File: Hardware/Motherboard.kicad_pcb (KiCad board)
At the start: 2 copper layers, 46 parts, among them J1 BME680, J2 Conn_01x05_Male, J3 Display_1, J4 Display_2, J5 Buttons, J6 USB, Q1 DMG3414U, SW1 Button_Plus, SW2 Button_Minus, SW3 Button_Settings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

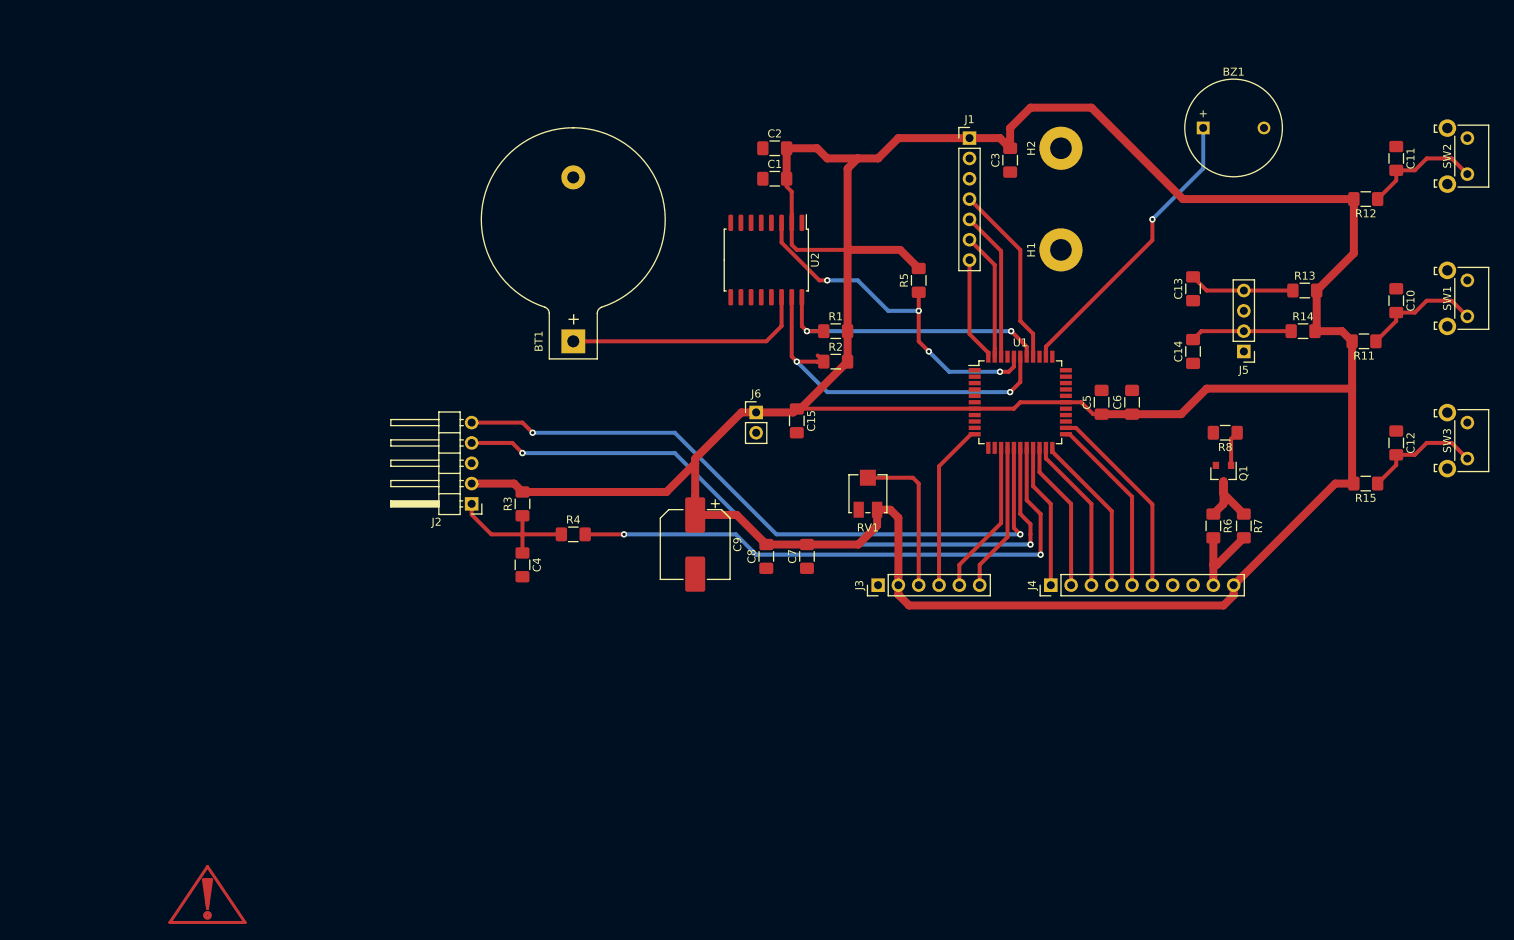
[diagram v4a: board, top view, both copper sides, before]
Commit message: [Hardware] Moved buttons to another schematic sheet and fully routed PCB.
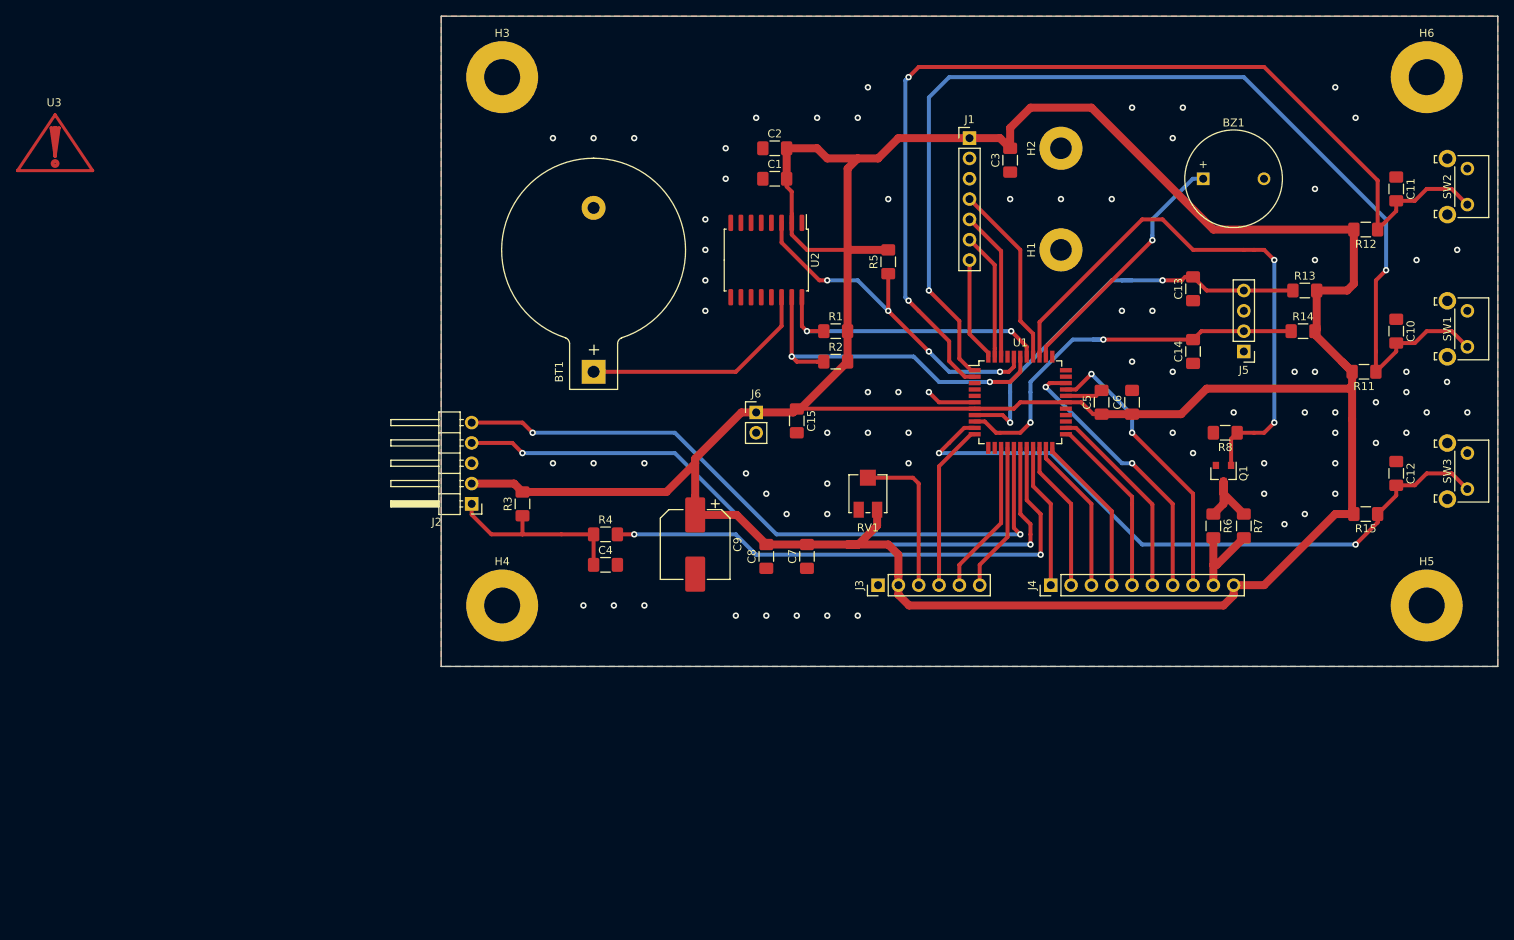
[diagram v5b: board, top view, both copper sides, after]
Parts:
- added H3: MountingHole_Pad, MountingHole:MountingHole_4.5mm_Pad, F.Cu at (128.3, 15.2)
- added H4: MountingHole_Pad, MountingHole:MountingHole_4.5mm_Pad, F.Cu at (128.3, 81.3)
- added H5: MountingHole_Pad, MountingHole:MountingHole_4.5mm_Pad, F.Cu at (243.8, 81.3)
- added H6: MountingHole_Pad, MountingHole:MountingHole_4.5mm_Pad, F.Cu at (243.8, 15.2)
- moved U3 95.9 mm to (72.4, 24.1)
- moved C4 10.4 mm to (141.2, 76.2), turned to 0 degrees
- moved BZ1 6.35 mm to (215.9, 27.9)
- moved BT1 4.58 mm to (139.7, 52.1)
- moved R5 4.46 mm to (176.5, 38.3)
- moved R4 4.03 mm to (141.2, 72.4)
- moved C10 3.81 mm to (240.0, 47.0)
- moved C11 3.81 mm to (240.0, 29.2)
- moved R11 3.81 mm to (236.0, 52.1)
- moved SW1 3.81 mm to (248.9, 44.5)
- moved SW2 3.81 mm to (248.9, 26.7)
- moved R12 3.81 mm to (236.2, 34.3)
- moved C12 3.81 mm to (240.0, 64.8)
- moved SW3 3.81 mm to (248.9, 62.2)
- moved R15 3.81 mm to (236.2, 69.8)
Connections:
- C10 pad 2: Net-(C10-Pad2) -> /PLUS_BUTTON
- C11 pad 2: Net-(C11-Pad2) -> /MINUS_BUTTON
- R11 pad 1: Net-(C10-Pad2) -> /PLUS_BUTTON
- R12 pad 1: Net-(C11-Pad2) -> /MINUS_BUTTON
- SW1 pad 2: Net-(C10-Pad2) -> /PLUS_BUTTON
- SW2 pad 2: Net-(C11-Pad2) -> /MINUS_BUTTON
- U1 pad 1: Net-(U1-Pad1) -> /PLUS_BUTTON
- U1 pad 2: Net-(U1-Pad2) -> /MINUS_BUTTON
- U1 pad 25: Net-(C11-Pad2) -> Net-(U1-Pad25)
- U1 pad 26: Net-(C10-Pad2) -> Net-(U1-Pad26)
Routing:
- net /PLUS_BUTTON: track 0.00 -> 136.8 mm, vias 0 -> 2
- net /MINUS_BUTTON: track 0.00 -> 128.0 mm, vias 0 -> 2
- net /SETTINGS_BUTTON: track 14.9 -> 82.4 mm, vias 0 -> 2
- net /DISPLAY_BACKLIGHT: track 4.39 -> 71.0 mm, vias 0 -> 2
- net /ALARM_BUTTON: track 13.2 -> 52.7 mm, vias 0 -> 2
- net /BACKLIGHT_BUTTON: track 12.7 -> 49.2 mm, vias 0 -> 2
- net /Display/DISPLAY_DB7: track 0.00 -> 35.7 mm, vias 0 -> 2
- net /Display/DISPLAY_DB6: track 0.00 -> 34.8 mm, vias 0 -> 2
- net Net-(C10-Pad2): track 15.0 -> 0.00 mm
- net Net-(C11-Pad2): track 14.9 -> 0.00 mm
- net GND: track 0.00 -> 11.0 mm, vias 0 -> 75
- net Net-(BZ1-Pad1): track 36.7 -> 31.1 mm
- net Net-(C4-Pad1): track 18.2 -> 23.7 mm
- net +5V: track 415.4 -> 411.3 mm
- net /RE3: track 72.1 -> 68.0 mm
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- added copper zone on B.Cu, net GND
- added copper zone on F.Cu, net GND
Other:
- board outline added: 132.1 x 81.3 mm

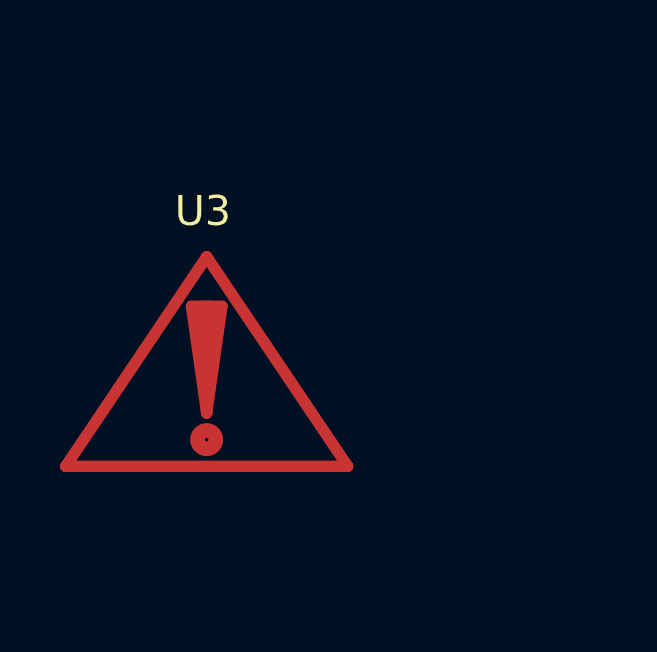
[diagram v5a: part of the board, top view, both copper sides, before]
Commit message: [Hardware] Used a custom empty footprint for Adafruit module part. This way, part is visible in schematic and bill of materials, but it is not part of the PCB.
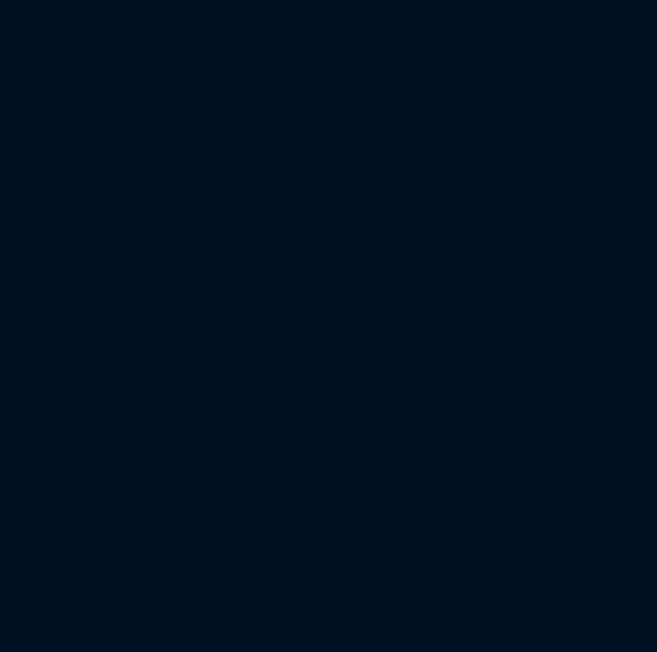
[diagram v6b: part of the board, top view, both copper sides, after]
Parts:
- U3: footprint Symbol:Symbol_Attention_CopperTop_Small -> Empty_Footprint:Empty_Footprint
- moved U3 6.84 mm to (78.7, 26.7)
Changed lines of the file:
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@@
   )
   (setup
-    (last_trace_width 1)
+    (last_trace_width 0.5)
     (user_trace_width 0.5)
     (user_trace_width 1)
@@
       (outputformat 1)
       (mirror false)
-      (drillshape 1)
+      (drillshape 0)
       (scaleselection 1)
-      (outputdirectory ""))
+      (outputdirectory "Clock 2/"))
   )
   (net 0 "")
@@
     (add_net "Net-(J4-Pad9)")
   )
+  (module Empty_Footprint:Empty_Footprint (layer F.Cu)
+    (at 78.74 26.67)
+    (fp_text reference U3 (at -3.81 6.35) (layer Eco1.User)
+      (effects (font (size 1 1) (thickness 0.15)))
+    )
+    (fp_text value Adafruit_BME680 (at 0 8.89) (layer Eco1.User)
+      (effects (font (size 1 1) (thickness 0.15)))
+    )
+    (fp_line (start 7.62 -3.81) (end -7.62 -3.81) (layer Eco1.User) (width 0.12))
+    (fp_line (start 7.62 5.08) (end 7.62 -3.81) (layer Eco1.User) (width 0.12))
+    (fp_line (start -7.62 5.08) (end 7.62 5.08) (layer Eco1.User) (width 0.12))
+    (fp_line (start -7.62 -3.81) (end -7.62 5.08) (layer Eco1.User) (width 0.12))
+  )
   (module MountingHole:MountingHole_4.5mm_Pad (layer F.Cu)
     (at 243.84 15.24)
@@
     (pad 1 thru_hole circle (at 0 0) (size 9 9) (drill 4.5) (layers *.Cu *.Mask)
       (net 47 "Net-(H3-Pad1)"))
-  )
-  (module Symbol:Symbol_Attention_CopperTop_Small (layer F.Cu)
-    (at 72.39 24.13)
-    (descr "Symbol, Attention, Copper Top, Small,")
-    (tags "Symbol, Attention, Copper Top, Small,")
-    (attr virtual)
-    (fp_text reference U3 (at -0.127 -5.715) (layer F.SilkS)
-      (effects (font (size 1 1) (thickness 0.15)))
-    )
-    (fp_text value Adafruit_BME680 (at -0.381 4.572) (layer F.Fab)
-      (effects (font (size 1 1) (thickness 0.15)))
-    )
-    (fp_line (start -0.508 -2.54) (end 0 -2.54) (layer F.Cu) (width 0.381))
-    (fp_line (start 0 1.016) (end -0.508 -2.54) (layer F.Cu) (width 0.381))
-    (fp_line (start 0.508 -2.54) (end 0 1.016) (layer F.Cu) (width 0.381))
-    (fp_line (start 0 -2.54) (end 0.508 -2.54) (layer F.Cu) (width 0.381))
-    (fp_line (start 0 0.889) (end 0.127 -2.54) (layer F.Cu) (width 0.381))
-    (fp_line (start 0 1.016) (end -0.127 -2.54) (layer F.Cu) (width 0.381))
-    (fp_circle (center 0 1.905) (end 0.254 2.159) (layer F.Cu) (width 0.381))
-    (fp_circle (center 0 1.905) (end 0 2.032) (layer F.Cu) (width 0.381))
-    (fp_line (start -4.699 2.794) (end 0 -4.191) (layer F.Cu) (width 0.381))
-    (fp_line (start 4.699 2.794) (end -4.699 2.794) (layer F.Cu) (width 0.381))
-    (fp_line (start 0 -4.191) (end 4.699 2.794) (layer F.Cu) (width 0.381))
   )
   (module MountingHole:MountingHole_2.7mm_Pad (layer F.Cu)
@@
   (segment (start 182.88 77.537919) (end 182.88 78.74) (width 0.5) (layer F.Cu) (net 41))
   (segment (start 187.34 59.88) (end 186.88 59.88) (width 0.5) (layer F.Cu) (net 41))
-  (segment (start 187.34 51.88) (end 186.88 51.88) (width 0.5) (layer F.Cu) (net 53))
   (segment (start 196.24 48.93) (end 209.55 35.62) (width 0.5) (layer F.Cu) (net 42))
   (segment (start 196.24 50.18) (end 196.24 48.93) (width 0.5) (layer F.Cu) (net 42))
@@
   (segment (start 209.55 35.054315) (end 209.55 35.62) (width 0.5) (layer B.Cu) (net 42))
   (segment (start 215.9 27.94) (end 214.6 27.94) (width 0.5) (layer B.Cu) (net 42))
-  (segment (start 240.03 48.4775) (end 242.3525 48.4775) (width 0.5) (layer F.Cu) (net 53))
-  (segment (start 242.3525 48.4775) (end 243.84 46.99) (width 0.5) (layer F.Cu) (net 53))
-  (segment (start 246.96 46.99) (end 248.92 48.95) (width 0.5) (layer F.Cu) (net 53))
-  (segment (start 243.84 46.99) (end 246.96 46.99) (width 0.5) (layer F.Cu) (net 53))
-  (segment (start 240.03 49.53) (end 237.49 52.07) (width 0.5) (layer F.Cu) (net 53))
-  (segment (start 240.03 48.4775) (end 240.03 49.53) (width 0.5) (layer F.Cu) (net 53))
-  (segment (start 240.03 30.6975) (end 242.3525 30.6975) (width 0.5) (layer F.Cu) (net 54))
-  (segment (start 242.3525 30.6975) (end 243.84 29.21) (width 0.5) (layer F.Cu) (net 54))
-  (segment (start 246.96 29.21) (end 248.92 31.17) (width 0.5) (layer F.Cu) (net 54))
-  (segment (start 243.84 29.21) (end 246.96 29.21) (width 0.5) (layer F.Cu) (net 54))
-  (segment (start 240.03 31.9675) (end 237.7075 34.29) (width 0.5) (layer F.Cu) (net 54))
-  (segment (start 240.03 30.6975) (end 240.03 31.9675) (width 0.5) (layer F.Cu) (net 54))
   (segment (start 240.03 67.5275) (end 237.7075 69.85) (width 0.5) (layer F.Cu) (net 43))
   (segment (start 240.03 66.2575) (end 240.03 67.5275) (width 0.5) (layer F.Cu) (net 43))
@@
   (segment (start 180.34 66.04) (end 180.34 78.74) (width 0.5) (layer F.Cu) (net 46))
   (segment (start 179.61 65.31) (end 180.34 66.04) (width 0.5) (layer F.Cu) (net 46))
+  (segment (start 187.34 51.88) (end 186.88 51.88) (width 0.5) (layer F.Cu) (net 53))
+  (segment (start 240.03 48.4775) (end 242.3525 48.4775) (width 0.5) (layer F.Cu) (net 53))
+  (segment (start 242.3525 48.4775) (end 243.84 46.99) (width 0.5) (layer F.Cu) (net 53))
+  (segment (start 246.96 46.99) (end 248.92 48.95) (width 0.5) (layer F.Cu) (net 53))
+  (segment (start 243.84 46.99) (end 246.96 46.99) (width 0.5) (layer F.Cu) (net 53))
+  (segment (start 240.03 49.53) (end 237.49 52.07) (width 0.5) (layer F.Cu) (net 53))
+  (segment (start 240.03 48.4775) (end 240.03 49.53) (width 0.5) (layer F.Cu) (net 53))
   (segment (start 237.49 52.07) (end 237.49 49.53) (width 0.5) (layer F.Cu) (net 53))
   (segment (start 237.49 49.53) (end 237.49 40.64) (width 0.5) (layer F.Cu) (net 53))
@@
   (segment (start 181.61 41.91) (end 181.61 17.78) (width 0.5) (layer B.Cu) (net 53))
   (segment (start 181.61 17.78) (end 184.15 15.24) (width 0.5) (layer B.Cu) (net 53))
+  (segment (start 240.03 30.6975) (end 242.3525 30.6975) (width 0.5) (layer F.Cu) (net 54))
+  (segment (start 242.3525 30.6975) (end 243.84 29.21) (width 0.5) (layer F.Cu) (net 54))
+  (segment (start 246.96 29.21) (end 248.92 31.17) (width 0.5) (layer F.Cu) (net 54))
+  (segment (start 243.84 29.21) (end 246.96 29.21) (width 0.5) (layer F.Cu) (net 54))
+  (segment (start 240.03 31.9675) (end 237.7075 34.29) (width 0.5) (layer F.Cu) (net 54))
+  (segment (start 240.03 30.6975) (end 240.03 31.9675) (width 0.5) (layer F.Cu) (net 54))
   (segment (start 237.7075 34.29) (end 237.7075 28.1575) (width 0.5) (layer F.Cu) (net 54))
   (segment (start 237.7075 28.1575) (end 223.52 13.97) (width 0.5) (layer F.Cu) (net 54))

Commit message: [Hardware] Added display part in both schematic and PCB.
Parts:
- added U4: DEM20485SYH-LY, Empty_Footprint:Empty_Footprint, F.Cu at (78.7, 44.5)
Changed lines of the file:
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@@
     (tracks 456)
     (zones 0)
-    (modules 50)
+    (modules 51)
     (nets 55)
   )
@@
   )
   (module Empty_Footprint:Empty_Footprint (layer F.Cu)
+    (at 78.74 44.45)
+    (fp_text reference U4 (at -3.81 6.35) (layer Eco1.User)
+      (effects (font (size 1 1) (thickness 0.15)))
+    )
+    (fp_text value DEM20485SYH-LY (at 0 8.89) (layer Eco1.User)
+      (effects (font (size 1 1) (thickness 0.15)))
+    )
+    (fp_line (start 7.62 -3.81) (end -7.62 -3.81) (layer Eco1.User) (width 0.12))
+    (fp_line (start 7.62 5.08) (end 7.62 -3.81) (layer Eco1.User) (width 0.12))
+    (fp_line (start -7.62 5.08) (end 7.62 5.08) (layer Eco1.User) (width 0.12))
+    (fp_line (start -7.62 -3.81) (end -7.62 5.08) (layer Eco1.User) (width 0.12))
+  )
+  (module Empty_Footprint:Empty_Footprint (layer F.Cu)
